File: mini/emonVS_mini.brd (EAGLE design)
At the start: 52 x 70 mm, 17 parts, among them J7 RJ45 Jack, J8 TERMINAL_BLOCK_2P, M1 275VAC, T1 ZMPT101B

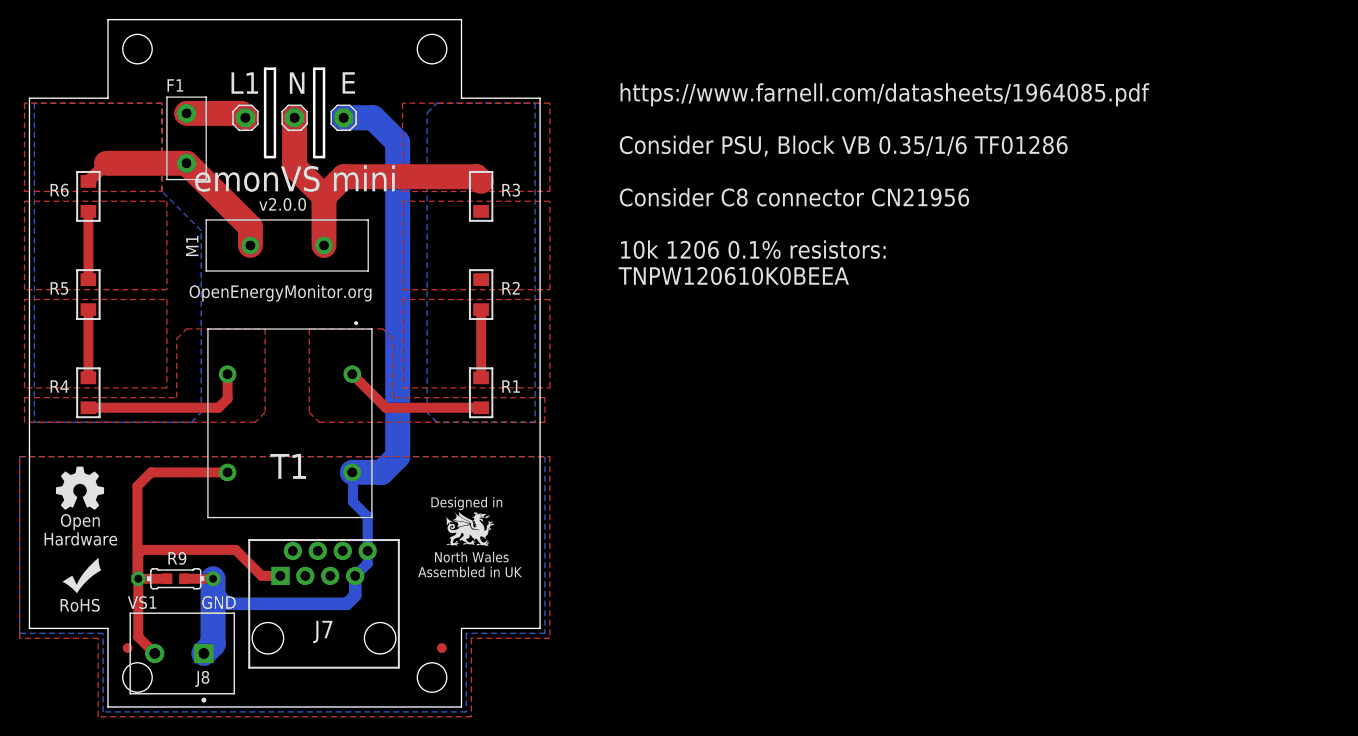
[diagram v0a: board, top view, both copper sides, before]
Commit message: improved thermal, swap around earth neutral, 0R link option
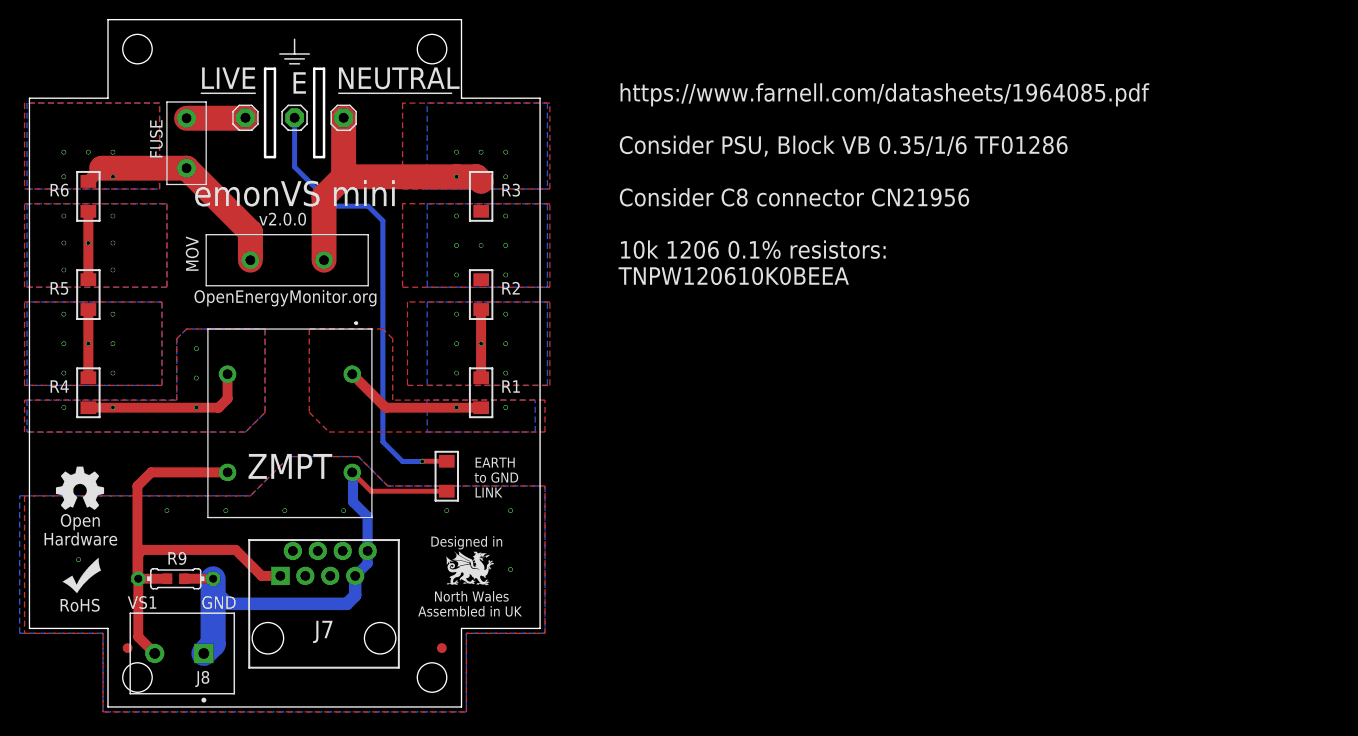
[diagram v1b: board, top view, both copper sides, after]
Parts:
- removed F1: 1A x 250V, OpenEnergyMonitor:FUSE
- removed M1: 275VAC, OpenEnergyMonitor:MOV
- added FUSE: 1A x 250V, OpenEnergyMonitor:FUSE
- added MOV: 275VAC, OpenEnergyMonitor:MOV
- added R7: 0R, My-RLC:R1206
- moved JP2 5.00 mm to (32.0, 60.0)
- moved JP3 5.00 mm to (27.0, 60.0)
- renumbered T1 to ZMPT
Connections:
- new net N$8: JP3.1, R7.2
- net GND: now also R7.1; no longer JP3.1
- net L1_VOLTAGE: now also FUSE.OUT, MOV.1; no longer F1.OUT, M1.1
- net N$7: now also FUSE.IN; no longer F1.IN
- net NEUTRAL: now also MOV.2; no longer M1.2
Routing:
- net N$8: track 0.00 -> 46.1 mm, vias 0 -> 1
- net GND: track 85.0 -> 51.6 mm, vias 0 -> 8
- net NEUTRAL: track 31.3 -> 29.5 mm, vias 0 -> 5
- net L1_VOLTAGE: track 21.8 -> 22.6 mm, vias 0 -> 5
- net N$5: vias 0 -> 7
- net N$4: vias 0 -> 7
- net N$3: vias 0 -> 7
- net N$2: vias 0 -> 2
- net N$1: vias 0 -> 5
- added copper zone on layer 16, net L1_VOLTAGE
- added copper zone on layer 16, net N$1
- added copper zone on layer 16, net N$2
- added copper zone on layer 16, net N$3
- added copper zone on layer 16, net N$4
- added copper zone on layer 16, net N$5
- added copper zone on layer 16, net N$6
- added copper zone on layer 16, net NEUTRAL
- removed copper zone on layer 16, net N$8
- removed copper zone on layer 16, net N$9
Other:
- board text added: "EARTH to GND LINK"
- board text added: "FUSE"
- board text added: "LIVE"
- board text added: "NEUTRAL"
- board text removed: "L1"
- board text removed: "N"
